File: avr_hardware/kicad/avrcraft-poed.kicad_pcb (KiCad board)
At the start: 2 copper layers, 50 x 50 mm, 58 parts, among them CN1 10p, CN2 .1u, CN3 10p, CN4 10n, J1 AVRISP6, P1 ETHERNET, P10 GND, P11 +5V, P12 GND, P13 GND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

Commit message: update POED for manufacture
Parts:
- added CN5: .1u, NETWORK0606, F.Cu at (64.1, 60.4)
- C1: value .22u -> NP
- CN2: footprint NETWORK1206 -> NETWORK0606
- H1, H2, H3, H4: value GND -> ?
- P16, P2, P3: moved to F.Cu
- U4: value A4447 -> A4447SLJTR
- moved CN2 19.9 mm to (41.5, 54.3), turned to 90 degrees
- moved P4 16.1 mm to (41.9, 65.4)
- moved P15 15.8 mm to (86.4, 66.6)
- moved P14 9.82 mm to (64.5, 62.9)
- moved P2 3.01 mm to (41.6, 57.7)
- moved RN3 2.95 mm to (60.4, 67.1)
- moved CN1 2.15 mm to (58.6, 53.2)
- moved X1 1.97 mm to (59.4, 54.7)
- moved P13 1.82 mm to (86.0, 55.4)
- moved D1 1.66 mm to (58.0, 81.6)
- moved P3 1.65 mm to (41.7, 60.2)
- moved CN4 1.46 mm to (60.4, 72.0)
- moved P12 1.46 mm to (85.3, 45.0)
- moved U2 1.41 mm to (61.0, 59.5)
- moved P11 1.06 mm to (71.9, 46.0)
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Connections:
- net N-0000027 renamed /PD2/INT0
- net N-0000029 renamed /PD5/OC0B
- net N-0000032 renamed /PB1/OC1A
- net N-0000078 renamed /PB0/CLKO
- CN2 pad 1: N-0000015 (its old number) -> GND
- CN2 pad 2: +3.3V -> +5V
- CN2 pad 3: +5V -> GND
- CN2 pad 4: +5V -> N-0000013
- P5 pad 1: N-0000033 -> /SDA/PC4/PD7
- P5 pad 3: N-0000028 -> /SCL/PC5/PD6/OC0A
- P8 pad 4: N-0000026 (its old number) -> /PD3/INT1/OC2B
- RN1 pad 1: N-0000033 -> +3.3V
- RN1 pad 2: +3.3V -> /SCL/PC5/PD6/OC0A
- RN1 pad 3: N-0000028 -> +3.3V
- RN1 pad 4: +3.3V -> /SDA/PC4/PD7
- U1 pad 1: N-0000026 (its old number) -> /PD3/INT1/OC2B
- U1 pad 10: N-0000033 -> /SCL/PC5/PD6/OC0A
- U1 pad 11: N-0000028 -> /SDA/PC4/PD7
- U1 pad 20: N-0000015 (its old number) -> N-0000013
- U1 pad 27: N-0000033 -> /SDA/PC4/PD7
- U1 pad 28: N-0000028 -> /SCL/PC5/PD6/OC0A
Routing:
- net N-0000033: track 31.0 -> 0.00 mm, vias 2 -> 0
- net /SDA/PC4/PD7: track 0.00 -> 29.6 mm
- net N-0000028: track 28.9 -> 0.00 mm, vias 3 -> 0
- net N-0000077: track 45.3 -> 17.6 mm
- net /SCL/PC5/PD6/OC0A: track 0.00 -> 26.5 mm
- net +3.3V: track 92.9 -> 69.7 mm, vias 2 -> 3
- net N-0000026 (its old number): track 23.0 -> 0.00 mm, vias 2 -> 0
- net /PD3/INT1/OC2B: track 0.00 -> 22.4 mm, vias 0 -> 2
- net N-0000015 (its old number): track 20.3 -> 0.00 mm, vias 2 -> 0
- net /POED: track 22.9 -> 9.57 mm
- net N-0000074: track 14.3 -> 26.2 mm
- net /POE+A: track 28.8 -> 36.4 mm, vias 2 -> 3
- net N-000005: track 17.5 -> 23.9 mm
- net /PB1/OC1A: track 14.3 -> 9.87 mm
- net GND: track 311.4 -> 307.1 mm, vias 9 -> 15
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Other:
- board text added: "3v3"
- board text added: "5V"
- board text added: "GND"
- board text added: "PB0/CLKO"
- board text added: "PB1/OC1A"
- board text added: "PD2/INT0"
- board text added: "PD3/OC2B"
- board text added: "PD5/OC0B"
- board text added: "SCL/PD6/OC0A"
- board text added: "SDA/PC4"

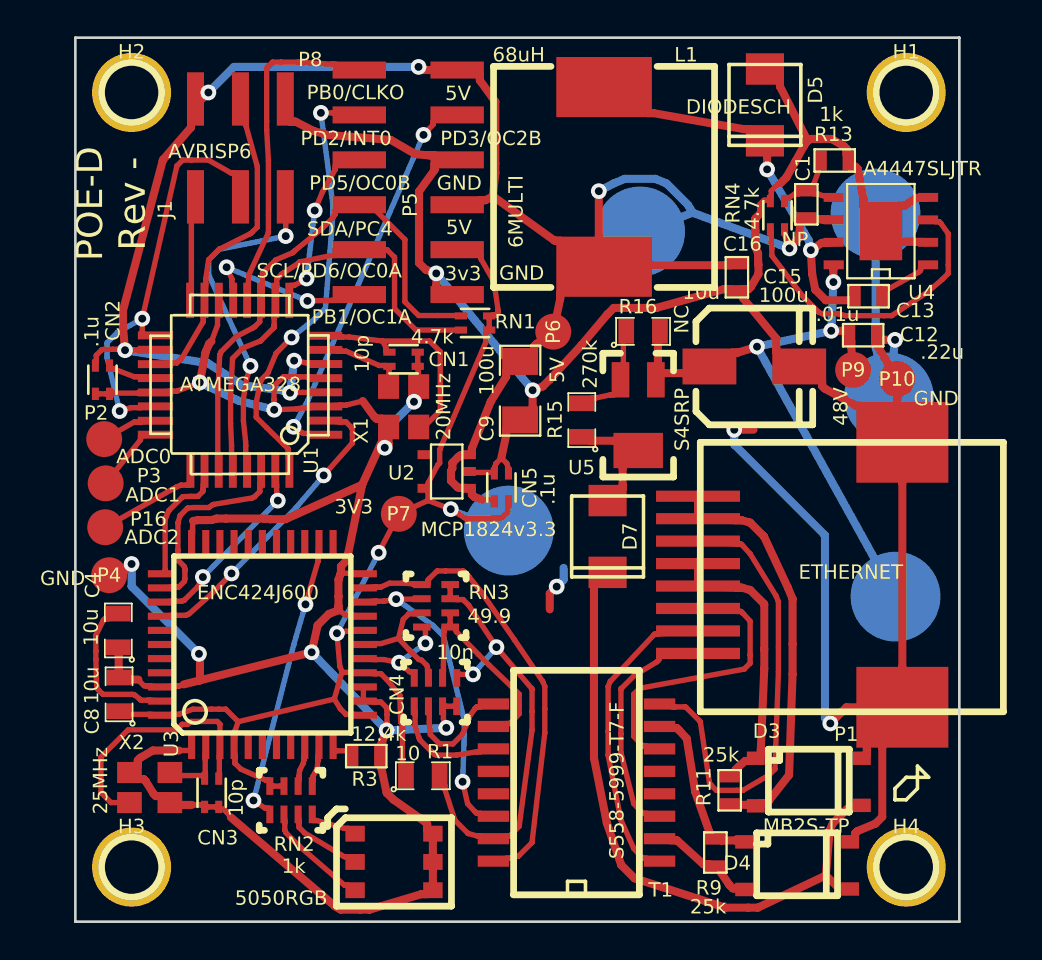
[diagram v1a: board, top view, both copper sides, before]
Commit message: Update for use with dedicated serial port.
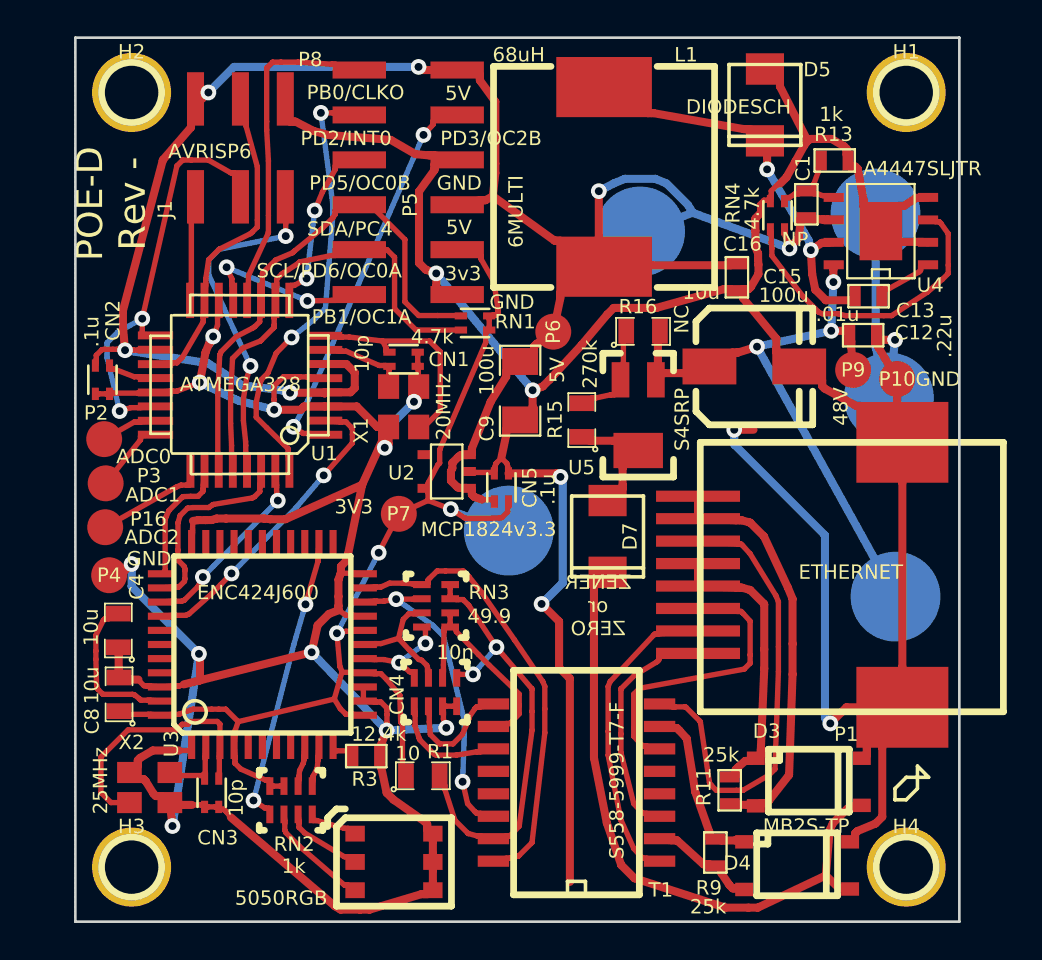
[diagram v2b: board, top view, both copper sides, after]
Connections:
- net N-0000012 renamed /RST
- net N-0000084 renamed /MOSI
- J1 pad 1: N-000002 (its old number) -> /MISO
- J1 pad 3: N-000005 (its old number) -> /SCK
- U1 pad 16: N-000002 (its old number) -> /MISO
- U1 pad 17: N-000005 (its old number) -> /SCK
- U1 pad 22: N-000005 (its old number) -> /SCK
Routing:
- net GND: track 307.1 -> 343.3 mm, vias 15 -> 18
- net N-000005 (its old number): track 23.9 -> 0.00 mm, vias 2 -> 0
- net /SCK: track 0.00 -> 23.9 mm, vias 0 -> 2
- net N-000002 (its old number): track 5.88 -> 0.00 mm
- net /MISO: track 0.00 -> 5.88 mm
- net +5V: track 119.5 -> 122.5 mm, vias 7 -> 6
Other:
- board text added: "ZENER or ZERO"

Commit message: changes - update with new design for LED
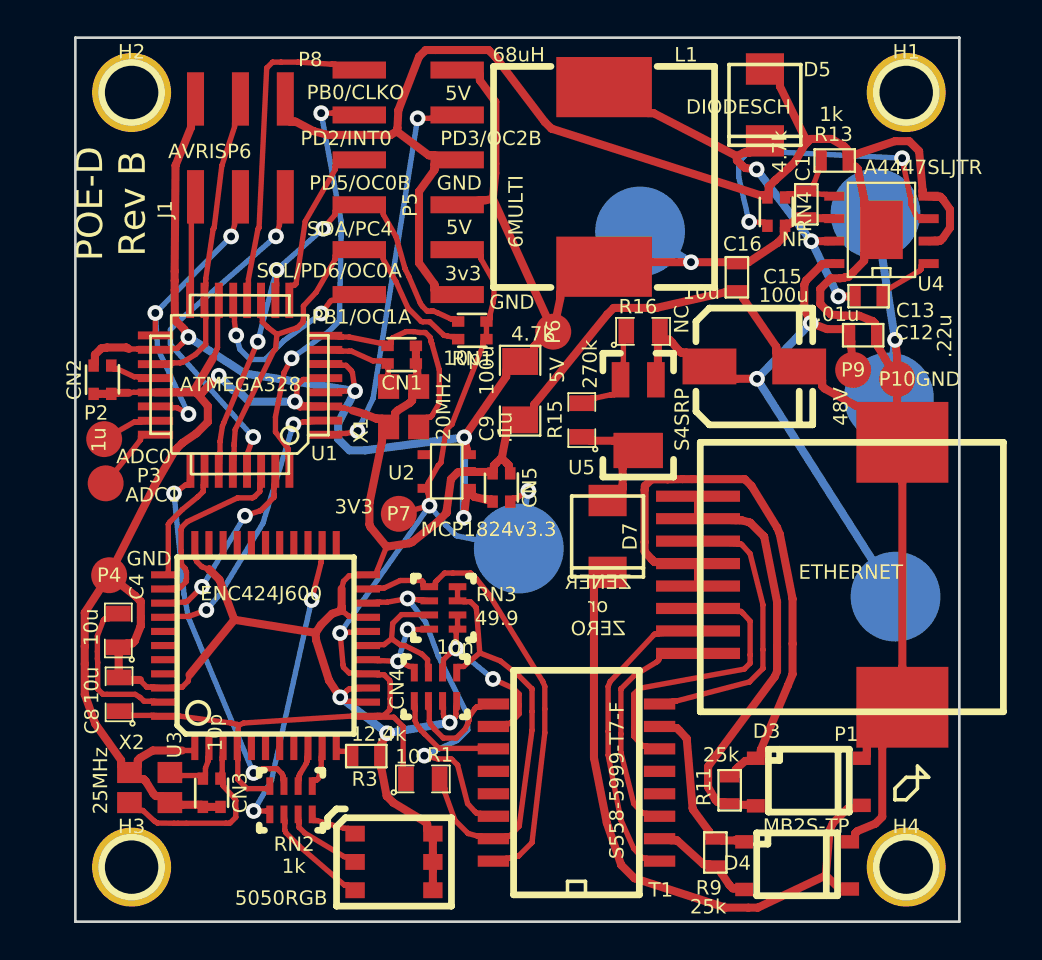
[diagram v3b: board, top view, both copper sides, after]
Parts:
- removed P16: ADC2, .1SMTPIN
- CN2: value .1u -> 1u
- moved P14 1.16 mm to (65.1, 63.9)
- moved RN1 0.44 mm to (62.5, 51.6)
- moved RN3 0.43 mm to (60.8, 67.3)
- moved CN4 0.30 mm to (60.4, 71.7)
- moved CN1 0.28 mm to (58.5, 52.9)
- moved RN4 0.22 mm to (79.6, 44.8)
- moved U3 0.19 mm to (50.8, 69.4)
- moved R1 0.18 mm to (59.7, 76.9)
- moved U4 0.08 mm to (85.6, 45.9)
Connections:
- P5 pad 1: /SDA/PC4/PD7 -> /SDA/PC4/OC0A
- P5 pad 3: /SCL/PC5/PD6/OC0A -> /SCL/PC5/PD7
- RN1 pad 2: /SCL/PC5/PD6/OC0A -> /SCL/PC5/PD7
- RN1 pad 4: /SDA/PC4/PD7 -> /SDA/PC4/OC0A
- RN2 pad 3: +3.3V -> BLUE
- U1 pad 10: /SCL/PC5/PD6/OC0A -> /SDA/PC4/OC0A
- U1 pad 11: /SDA/PC4/PD7 -> /SCL/PC5/PD7
- U1 pad 25: N-0000020 (its old number) -> BLUE
- U1 pad 27: /SDA/PC4/PD7 -> /SDA/PC4/OC0A
- U1 pad 28: /SCL/PC5/PD6/OC0A -> /SCL/PC5/PD7
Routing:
- net /SDA/PC4/PD7: track 29.6 -> 0.00 mm
- net /SDA/PC4/OC0A: track 0.00 -> 29.4 mm, vias 0 -> 3
- net GND: track 343.3 -> 316.3 mm, vias 18 -> 6
- net /SCL/PC5/PD6/OC0A: track 26.5 -> 0.00 mm
- net /SCL/PC5/PD7: track 0.00 -> 26.2 mm
- net BLUE: track 0.00 -> 21.0 mm, vias 0 -> 2
- net +5V: track 122.5 -> 104.4 mm, vias 6 -> 5
- net /POEB: track 16.3 -> 33.1 mm
- net N-0000064: track 26.2 -> 16.1 mm
- net N-0000020 (its old number): track 6.22 -> 0.00 mm
- net /SCK: track 23.9 -> 17.7 mm, vias 2 -> 3
- net N-0000061: track 14.6 -> 10.9 mm
- net N-0000032: track 18.1 -> 20.8 mm
- net +3.3V: track 69.7 -> 72.1 mm
- net N-0000019: track 17.5 -> 15.9 mm
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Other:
- net class Default: clearance 0.2794 -> 0.2286
- net class Power: clearance 0.2794 -> 0.2286
- rule trace_clearance: 0.2794 -> 0.2286
- board text added: "POE-D Rev B"
- board text removed: "POE-D Rev -"
